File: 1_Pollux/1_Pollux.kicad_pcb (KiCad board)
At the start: 2 copper layers, 154.4 x 172.8 mm, 207 parts, among them J1 Conn_01x02, SW1 Battery Switch, SW2 LED Switch, SW3 Reset Switch, U1 Nice_Nano_V2

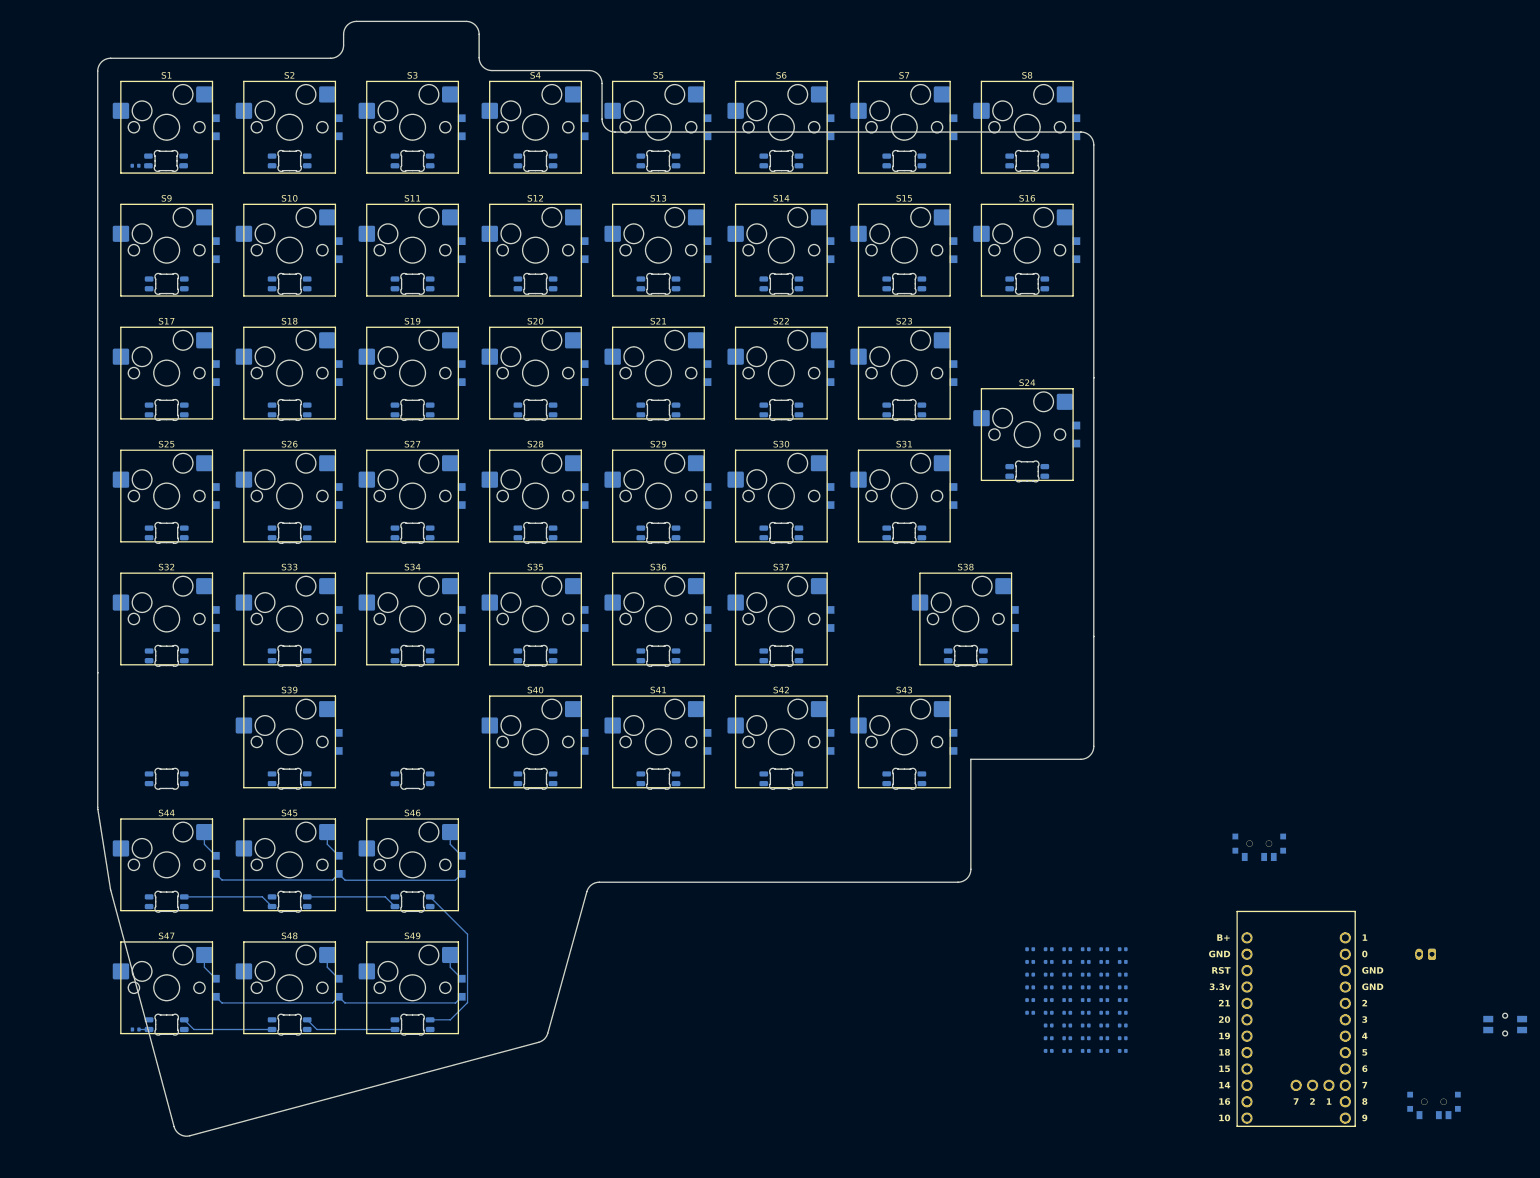
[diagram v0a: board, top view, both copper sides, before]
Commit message: feat: finish Pollux PCB | chore: generate gerber files for both sides
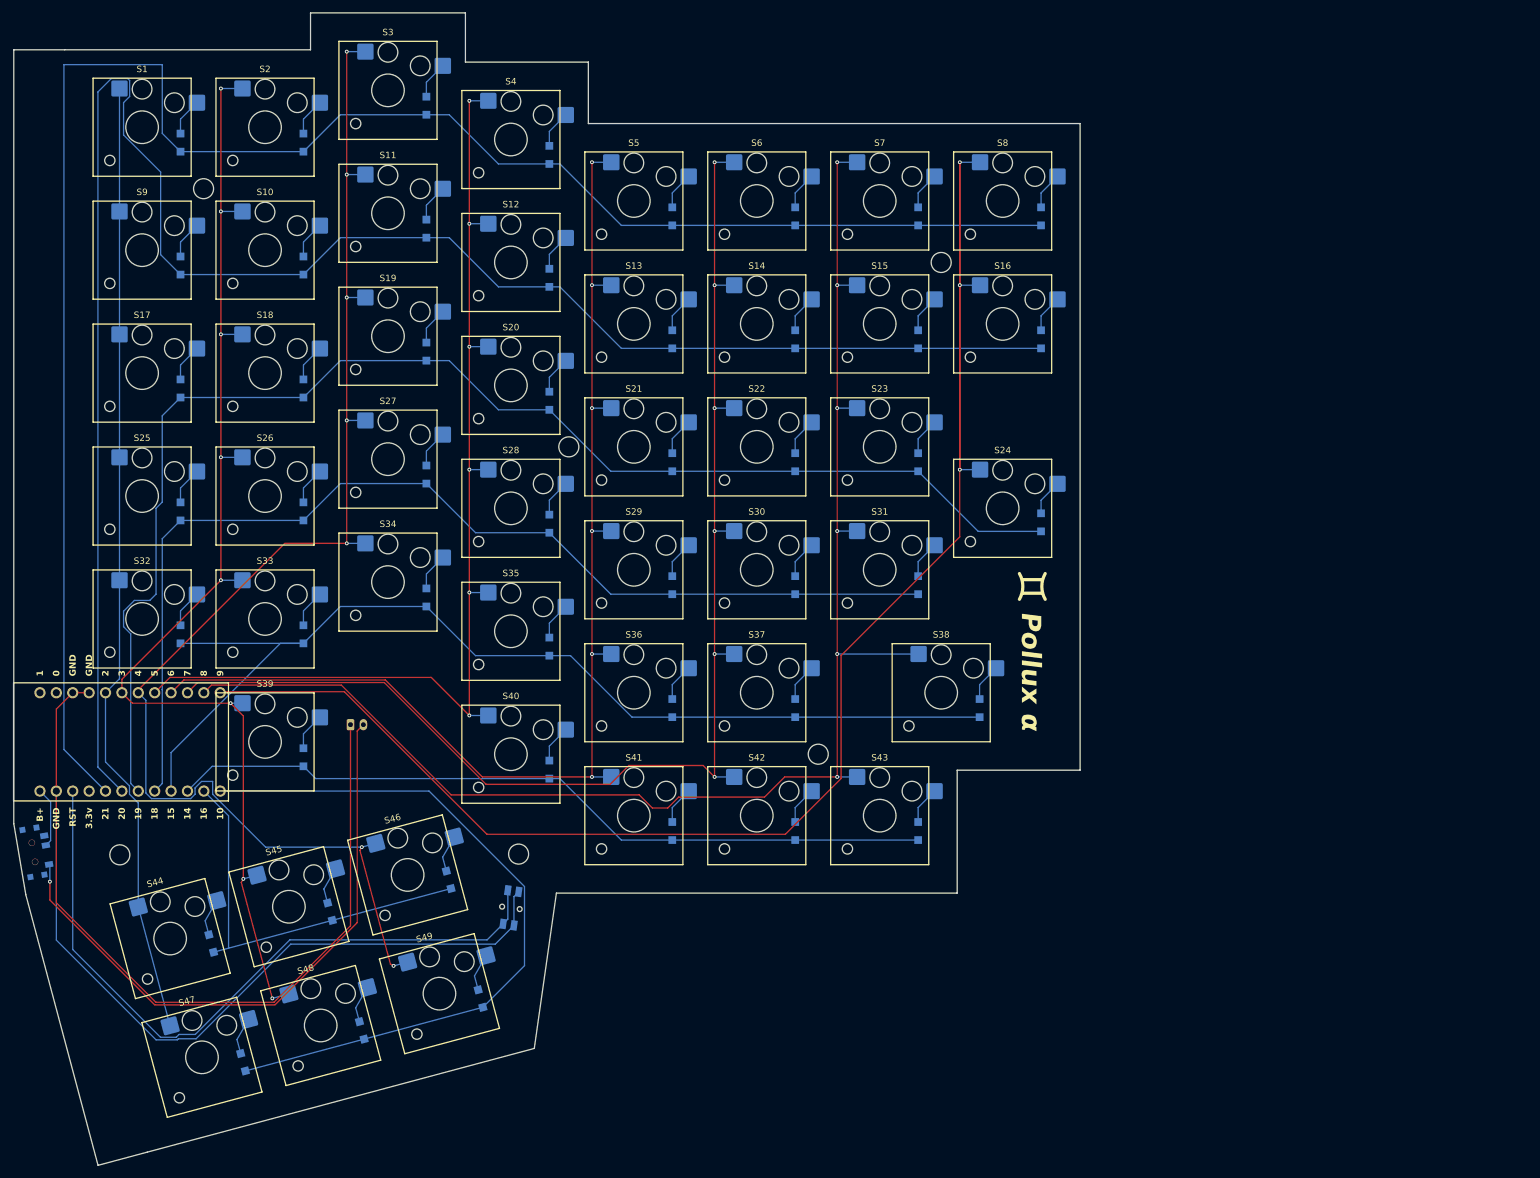
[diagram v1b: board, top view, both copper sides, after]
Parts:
- removed C1, C10, C11, C12, C13, C14, C15, C16, C17, C18, C19, C2, C20, C21, C22, C23, C24, C25, C26, C27, C28, C29, C3, C30, C31, C32, C33, C34, C35, C36, C37, C38, C39, C4, C40, C41, C42, C43, C44, C45, C46, C47, C48, C49, C5, C50, C51, C6, C7, C8, C9: 100nF, Capacitor_SMD:C_0402_1005Metric
- removed LED1, LED10, LED11, LED12, LED13, LED14, LED15, LED16, LED17, LED18, LED19, LED2, LED20, LED21, LED22, LED23, LED24, LED25, LED26, LED27, LED28, LED29, LED3, LED30, LED31, LED32, LED33, LED34, LED35, LED36, LED37, LED38, LED39, LED4, LED40, LED41, LED42, LED43, LED44, LED45, LED46, LED47, LED48, LED49, LED5, LED50, LED51, LED6, LED7, LED8, LED9: SK6812MINI-E, LED_SMD:LED_SK6812MINI-E_3.2x2.8mm_P1.5mm_ReverseMount
- removed R1, R2: 500Ω, Resistor_SMD:R_0402_1005Metric
- removed SW3: Reset Switch, Button_Switch_SMD:Panasonic_EVQPUL_EVQPUC
- added REF**: Mounting Hole, AstralExtensions:Mounting Hole, F.Cu at (100.4, 87.6)
- added REF**: Mounting Hole, AstralExtensions:Mounting Hole, F.Cu at (139.1, 135.3)
- added REF**: Mounting Hole, AstralExtensions:Mounting Hole, F.Cu at (92.6, 150.7)
- added REF**: Mounting Hole, AstralExtensions:Mounting Hole, F.Cu at (158.1, 59.1)
- added REF**: Mounting Hole, AstralExtensions:Mounting Hole, F.Cu at (43.8, 47.6)
- added REF**: Mounting Hole, AstralExtensions:Mounting Hole, F.Cu at (30.8, 150.8)
- S1, S10, S11, S12, S13, S14, S15, S16, S17, S18, S19, S2, S20, S21, S22, S23, S25, S26, S27, S28, S29, S3, S30, S31, S32, S33, S34, S35, S36, S37, S4, S40, S41, S42, S43, S44, S45, S46, S47, S48, S49, S5, S6, S7, S8, S9: footprint ScottoKeebs_Hotswap:Hotswap_MX_1.00u -> ScottoKeebs_Hotswap:Hotswap_Choc_V2_1.00u
- S24: footprint ScottoKeebs_Hotswap:Hotswap_MX_1.00u -> ScottoKeebs_Hotswap:Hotswap_Choc_V2_2.00u_90deg
- S38: footprint ScottoKeebs_Hotswap:Hotswap_MX_2.00u -> ScottoKeebs_Hotswap:Hotswap_Choc_V2_2.00u
- S39: footprint ScottoKeebs_Hotswap:Hotswap_MX_3.00u -> ScottoKeebs_Hotswap:Hotswap_Choc_V2_3.00u
- SW2: value LED Switch -> Reset Switch; footprint davidphilipbarr:SPDT_C128955 -> Button_Switch_SMD:Panasonic_EVQPUL_EVQPUC
- moved SW1 220.4 mm to (17.5, 150.5), turned to -80.4 degrees
- moved U1 186.3 mm to (32.1, 133.3), turned to -90 degrees
- moved J1 171.3 mm to (66.6, 130.7), turned to 0 degrees
- moved SW2 116.4 mm to (91.4, 159.1), turned to 82.02 degrees
- moved D36 14.9 mm to (116.4, 128.1)
- moved D37 14.9 mm to (135.5, 128.1)
- moved D13 14.9 mm to (116.4, 71.0)
- moved D14 14.9 mm to (135.5, 71.0)
- moved D15 14.9 mm to (154.5, 71.0)
- moved D16 14.9 mm to (173.6, 71.0)
- moved D38 14.9 mm to (164.1, 128.1)
- moved D21 14.9 mm to (116.4, 90.0)
- moved D22 14.9 mm to (135.5, 90.0)
- moved D23 14.9 mm to (154.5, 90.0)
- moved D29 14.9 mm to (116.4, 109.1)
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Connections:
- SW1 pad 2: /RAW -> +3.7V_{Battery}
- SW2 pad 1: /RAW -> GND
- SW2 pad 2: VDD -> /RST
- U1 pad 1: /LED IN -> unconnected-(U1-Pad1)
- U1 pad 24: /RAW -> +3.7V_{Battery}
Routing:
- net /Row 1: track 0.00 -> 292.7 mm
- net /Row 0: track 0.00 -> 287.9 mm
- net /Column 7: track 0.00 -> 269.1 mm, vias 0 -> 3
- net GND: track 0.00 -> 237.4 mm
- net /Column 6: track 0.00 -> 231.8 mm, vias 0 -> 6
- net /Row 2: track 0.00 -> 213.7 mm
- net /Column 2: track 0.00 -> 213.6 mm, vias 0 -> 7
- net /Column 5: track 0.00 -> 204.3 mm, vias 0 -> 6
- net /Column 1: track 0.00 -> 188.2 mm, vias 0 -> 8
- net /Column 4: track 0.00 -> 185.5 mm, vias 0 -> 6
- net /Row 3: track 0.00 -> 167.4 mm
- net /Row 4: track 0.00 -> 166.8 mm
- net /Column 3: track 0.00 -> 165.1 mm, vias 0 -> 6
- net /Column 0: track 0.00 -> 148.9 mm
- net /Row 5: track 0.00 -> 119.5 mm
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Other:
- board size 154.4 x 172.8 mm -> 165.2 x 178.6 mm
- board text added: "Pollux α"
